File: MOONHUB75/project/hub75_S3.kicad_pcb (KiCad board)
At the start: 2 copper layers, 50 x 48 mm, 15 parts, among them J1 Conn_01x08_Pin, J10 Conn_01x07_Pin, J11 Conn_02x05_Odd_Even, J2 Conn_01x08_Pin, J3 Conn_01x08_Pin, J4 Conn_01x02, J5 Conn_01x02, J6 Conn_01x06_Pin, J7 Conn_01x03_Pin, J8 Conn_01x03_Pin

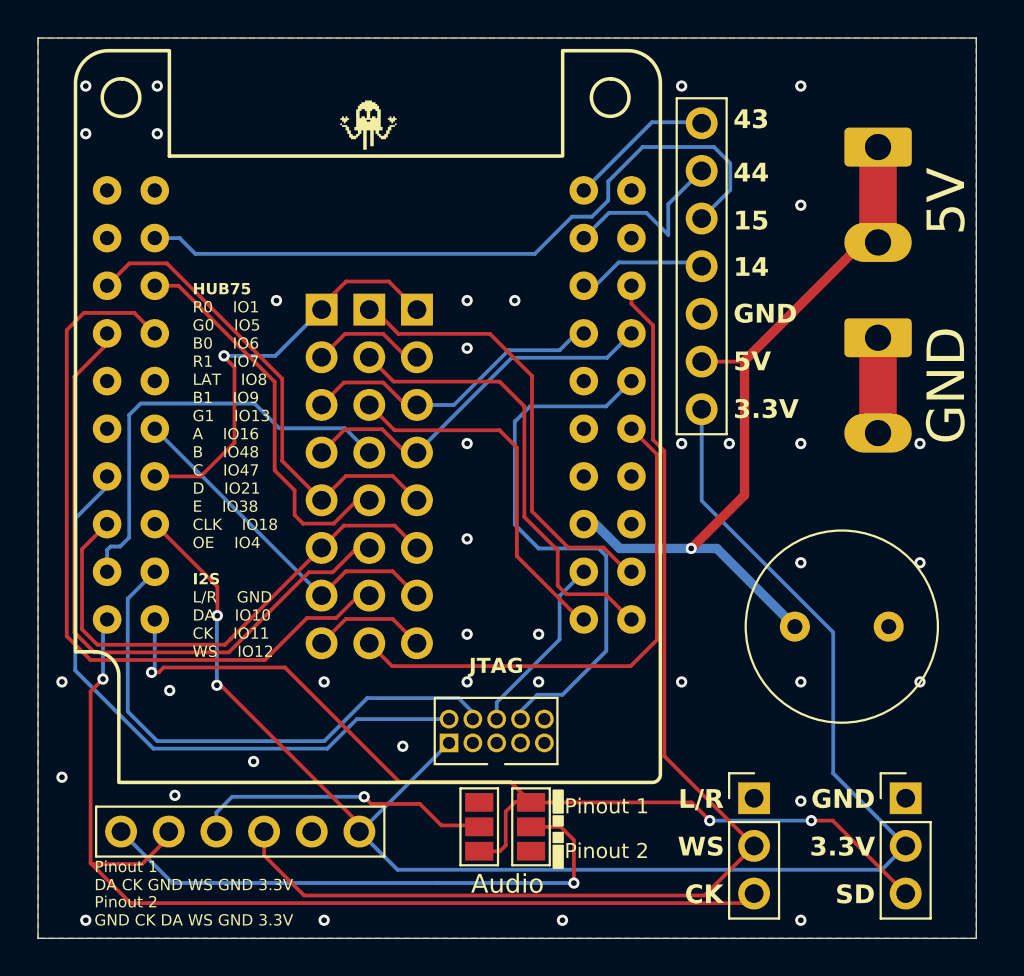
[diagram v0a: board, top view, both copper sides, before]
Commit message: Updated the PCB
Moved the pinheader of the HUB Panel to line up in the grid of the T7S3.
Added polarity marking on the capacitor
Added 3mm mounting holes
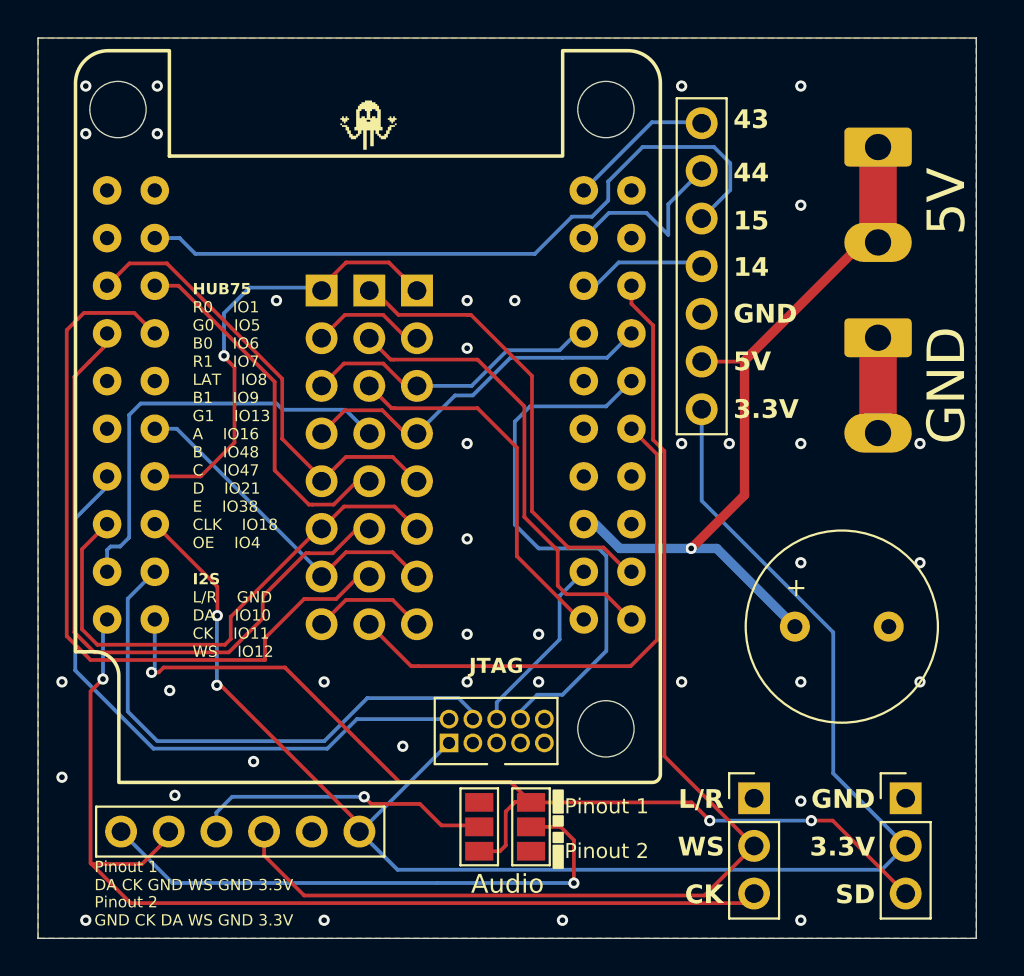
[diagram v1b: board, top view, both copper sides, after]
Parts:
- moved J1 1.01 mm to (133.1, 66.3)
- moved J2 1.01 mm to (135.6, 66.3)
- moved J3 1.01 mm to (138.1, 66.3)
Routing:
- net G0: track 23.0 -> 24.8 mm
- net A: track 20.7 -> 19.5 mm
- net D: track 27.5 -> 28.7 mm
- net B: track 25.9 -> 24.7 mm
- net CLK: track 39.9 -> 41.0 mm
- net C: track 35.1 -> 36.2 mm
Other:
- outline, holes or cut-outs redrawn
